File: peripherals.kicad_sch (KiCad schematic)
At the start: 14 parts, among them U5 FT230XQ

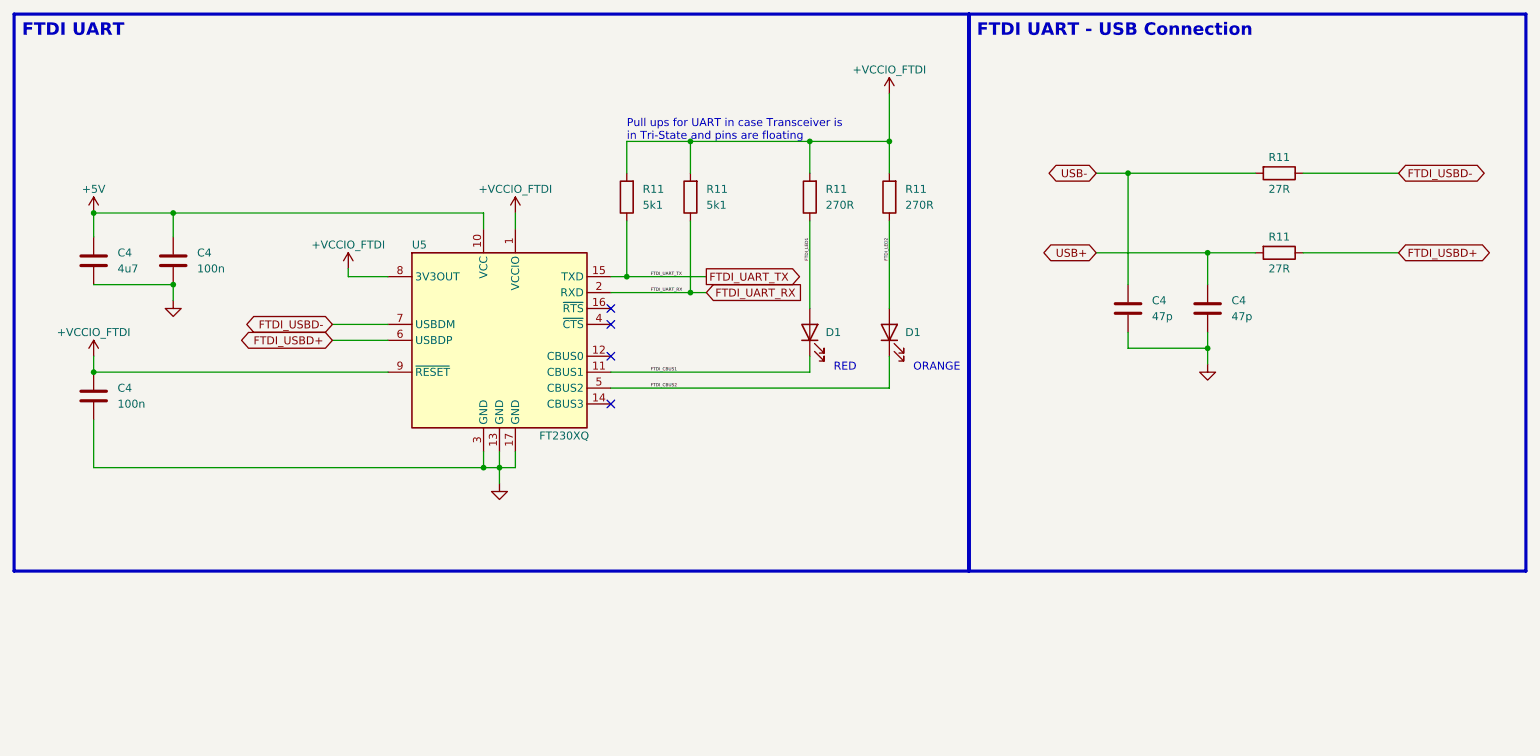
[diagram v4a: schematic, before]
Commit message: Added capacitor voltage rating
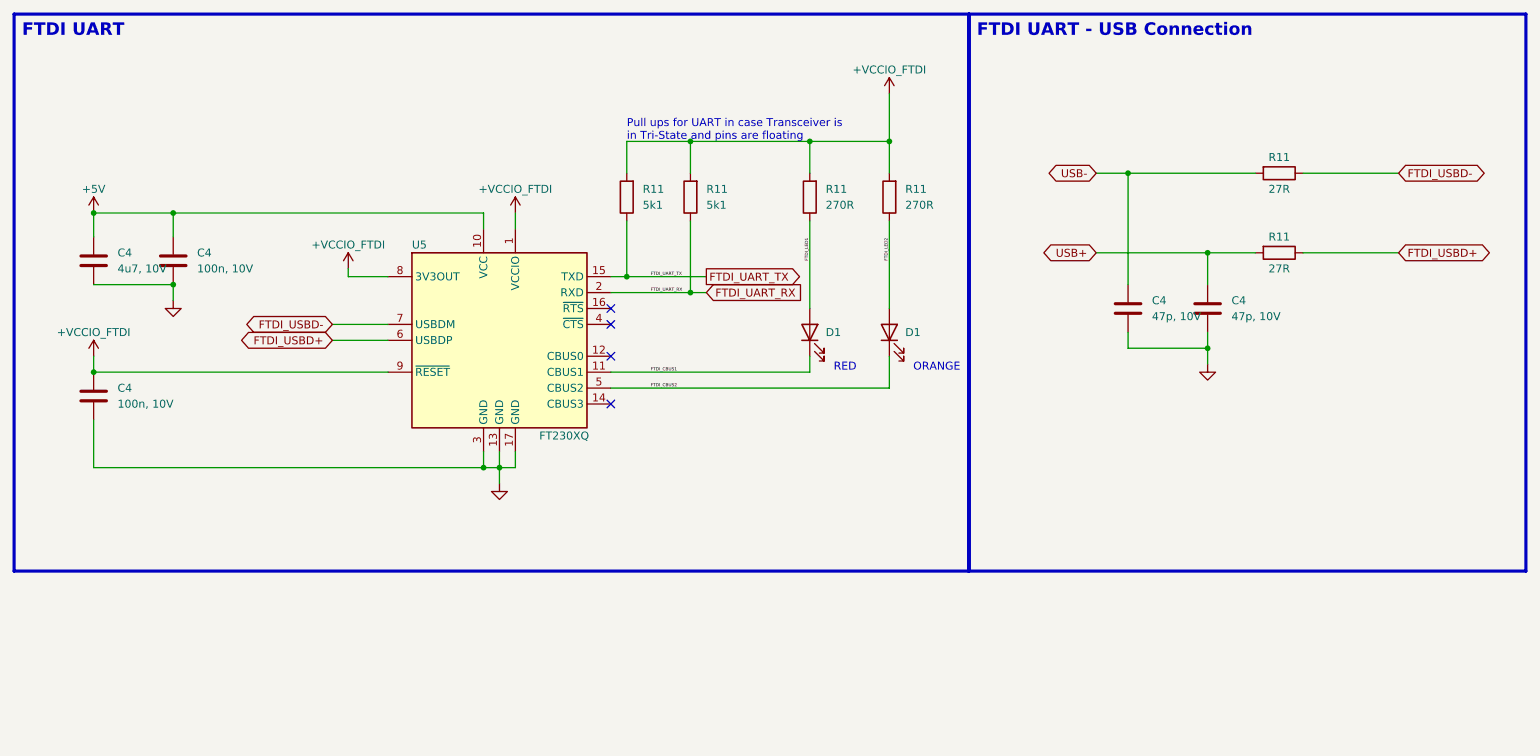
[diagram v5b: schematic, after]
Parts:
- C4: value 100n -> 100n, 10V
- C4: value 47p -> 47p, 10V
- C4: value 4u7 -> 4u7, 10V
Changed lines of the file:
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@@
       (effects (font (size 1.27 1.27)) (justify left))
     )
-    (property "Value" "100n" (at 41.91 87.63 0)
+    (property "Value" "100n, 10V" (at 41.91 87.63 0)
       (effects (font (size 1.27 1.27)) (justify left))
     )
@@
       (effects (font (size 1.27 1.27)) (justify left))
     )
-    (property "Value" "47p" (at 207.01 73.66 0)
+    (property "Value" "47p, 10V" (at 207.01 73.66 0)
       (effects (font (size 1.27 1.27)) (justify left))
     )
@@
       (effects (font (size 1.27 1.27)) (justify left))
     )
-    (property "Value" "47p" (at 219.71 73.66 0)
+    (property "Value" "47p, 10V" (at 219.71 73.66 0)
       (effects (font (size 1.27 1.27)) (justify left))
     )
@@
       (effects (font (size 1.27 1.27)) (justify left))
     )
-    (property "Value" "4u7" (at 41.91 66.04 0)
+    (property "Value" "4u7, 10V" (at 41.91 66.04 0)
       (effects (font (size 1.27 1.27)) (justify left))
     )
@@
       (effects (font (size 1.27 1.27)) (justify left))
     )
-    (property "Value" "100n" (at 54.61 66.04 0)
-      (effects (font (size 1.27 1.27)) (justify left))
-    )
+    (property "Value" "100n, 10V" (at 54.61 66.04 0)
+      (effects (font (size 1.27 1.27)) (justify left))
+    )
